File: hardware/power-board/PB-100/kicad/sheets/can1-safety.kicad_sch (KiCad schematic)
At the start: 0 parts

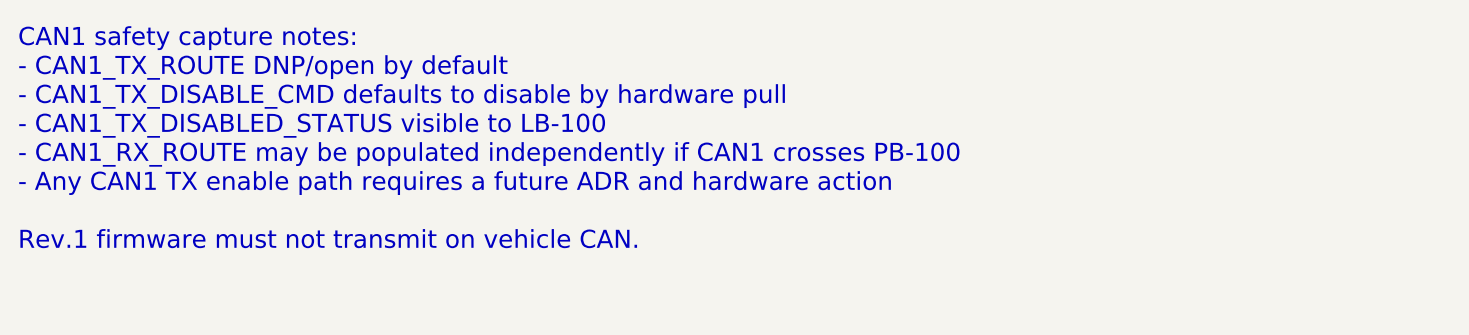
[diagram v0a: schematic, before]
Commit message: hardware: tighten pb100 can1 disable contract
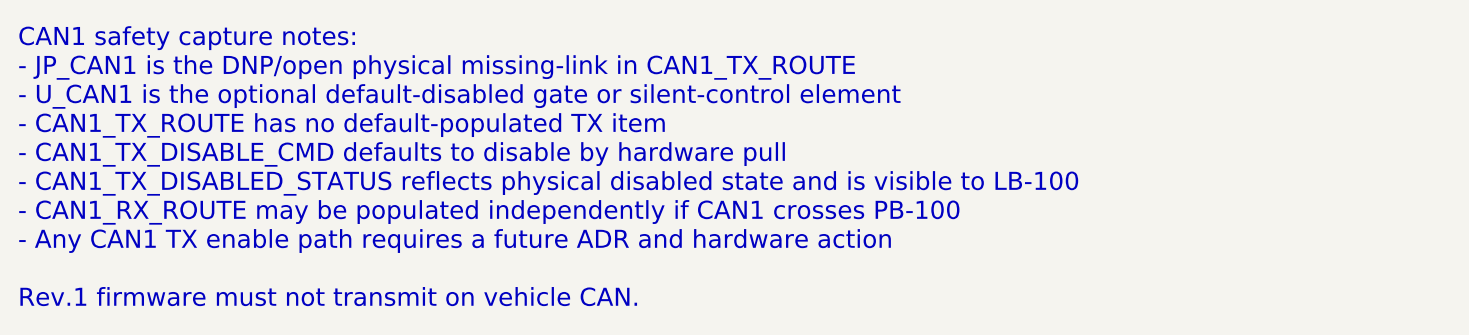
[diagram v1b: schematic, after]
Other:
- note added: "CAN1 safety capture notes: - JP_CAN1 is the DNP/open physical missing-link in CAN1_TX_ROUTE - U_CAN1 is the optional default-disabled gate or silent-control element - CAN1_TX_ROUTE has no default-populated TX item - CAN1_TX_DISABLE_CMD defaults to disable by hardware pull - CAN1_TX_DISABLED_STATUS reflects physical disabled state and is visible to LB-100 - CAN1_RX_ROUTE may be populated independe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"
- note removed: "CAN1 safety capture notes: - CAN1_TX_ROUTE DNP/open by default - CAN1_TX_DISABLE_CMD defaults to disable by hardware pull - CAN1_TX_DISABLED_STATUS visible to LB-100 - CAN1_RX_ROUTE may be populated independently if CAN1 crosses PB-100 - Any CAN1 TX enable path requires a future ADR and hardware action Rev.1 firmware must not transmit on vehicle CAN."
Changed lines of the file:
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@@
     (company "SVC Platform")
     (comment 9 "Work queue: CAP-CAN1. CAN1 capture keeps TX DNP/open and future ADR only.")
-    (comment 1 "Placeholder sheet. Capture CAN1 TX disable/DNP-open path here.")
+    (comment 1 "Capture contract: JP_CAN1 DNP/open TX link and U_CAN1 default-disabled gate.")
     (comment 2 "Source: PB-100-can1-tx-disable.md.")
   )
-  (text "CAN1 safety capture notes:\n- CAN1_TX_ROUTE DNP/open by default\n- CAN1_TX_DISABLE_CMD defaults to disable by hardware pull\n- CAN1_TX_DISABLED_STATUS visible to LB-100\n- CAN1_RX_ROUTE may be populated independently if CAN1 crosses PB-100\n- Any CAN1 TX enable path requires a future ADR and hardware action\n\nRev.1 firmware must not transmit on vehicle CAN."
+  (text "CAN1 safety capture notes:\n- JP_CAN1 is the DNP/open physical missing-link in CAN1_TX_ROUTE\n- U_CAN1 is the optional default-disabled gate or silent-control element\n- CAN1_TX_ROUTE has no default-populated TX item\n- CAN1_TX_DISABLE_CMD defaults to disable by hardware pull\n- CAN1_TX_DISABLED_STATUS reflects physical disabled state and is visible to LB-100\n- CAN1_RX_ROUTE may be populated independently if CAN1 crosses PB-100\n- Any CAN1 TX enable path requires a future ADR and hardware action\n\nRev.1 firmware must not transmit on vehicle CAN."
     (at 25 30 0)
     (effects (font (size 2.0 2.0)) (justify left top))

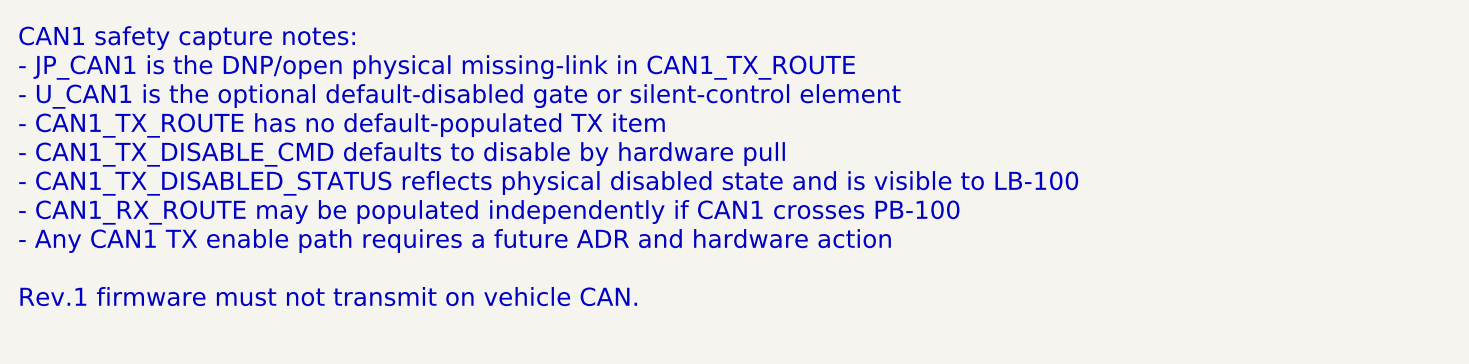
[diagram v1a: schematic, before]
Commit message: hardware: sync pb100 kicad sheet trace notes
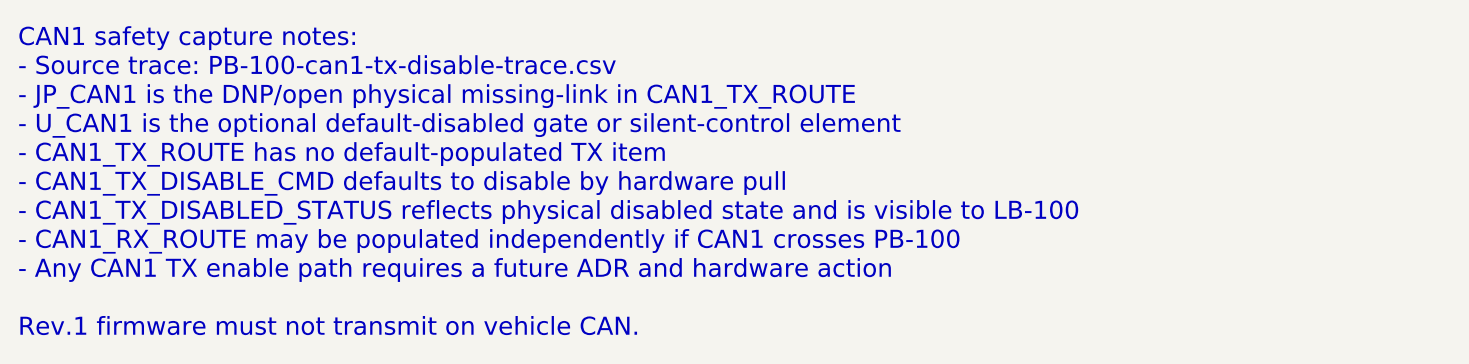
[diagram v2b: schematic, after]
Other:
- note added: "CAN1 safety capture notes: - Source trace: PB-100-can1-tx-disable-trace.csv - JP_CAN1 is the DNP/open physical missing-link in CAN1_TX_ROUTE - U_CAN1 is the optional default-disabled gate or silent-control element - CAN1_TX_ROUTE has no default-populated TX item - CAN1_TX_DISABLE_CMD defaults to disable by hardware pull - CAN1_TX_DISABLED_STATUS reflects physical disabled state and is visible to 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"
- note removed: "CAN1 safety capture notes: - JP_CAN1 is the DNP/open physical missing-link in CAN1_TX_ROUTE - U_CAN1 is the optional default-disabled gate or silent-control element - CAN1_TX_ROUTE has no default-populated TX item - CAN1_TX_DISABLE_CMD defaults to disable by hardware pull - CAN1_TX_DISABLED_STATUS reflects physical disabled state and is visible to LB-100 - CAN1_RX_ROUTE may be populated independe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"
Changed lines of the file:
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@@
     (comment 9 "Work queue: CAP-CAN1. CAN1 capture keeps TX DNP/open and future ADR only.")
     (comment 1 "Capture contract: JP_CAN1 DNP/open TX link and U_CAN1 default-disabled gate.")
-    (comment 2 "Source: PB-100-can1-tx-disable.md.")
+    (comment 2 "Sources: PB-100-can1-tx-disable-trace.csv and PB-100-can1-tx-disable.md.")
   )
-  (text "CAN1 safety capture notes:\n- JP_CAN1 is the DNP/open physical missing-link in CAN1_TX_ROUTE\n- U_CAN1 is the optional default-disabled gate or silent-control element\n- CAN1_TX_ROUTE has no default-populated TX item\n- CAN1_TX_DISABLE_CMD defaults to disable by hardware pull\n- CAN1_TX_DISABLED_STATUS reflects physical disabled state and is visible to LB-100\n- CAN1_RX_ROUTE may be populated independently if CAN1 crosses PB-100\n- Any CAN1 TX enable path requires a future ADR and hardware action\n\nRev.1 firmware must not transmit on vehicle CAN."
+  (text "CAN1 safety capture notes:\n- Source trace: PB-100-can1-tx-disable-trace.csv\n- JP_CAN1 is the DNP/open physical missing-link in CAN1_TX_ROUTE\n- U_CAN1 is the optional default-disabled gate or silent-control element\n- CAN1_TX_ROUTE has no default-populated TX item\n- CAN1_TX_DISABLE_CMD defaults to disable by hardware pull\n- CAN1_TX_DISABLED_STATUS reflects physical disabled state and is visible to LB-100\n- CAN1_RX_ROUTE may be populated independently if CAN1 crosses PB-100\n- Any CAN1 TX enable path requires a future ADR and hardware action\n\nRev.1 firmware must not transmit on vehicle CAN."
     (at 25 30 0)
     (effects (font (size 2.0 2.0)) (justify left top))

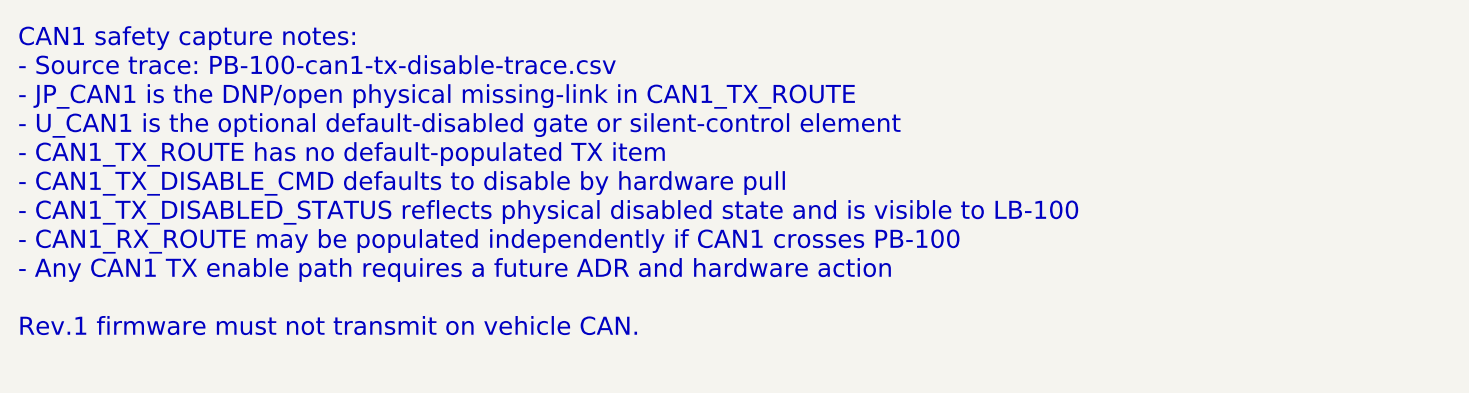
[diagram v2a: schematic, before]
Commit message: hardware: add pb100 can1 dnp production review
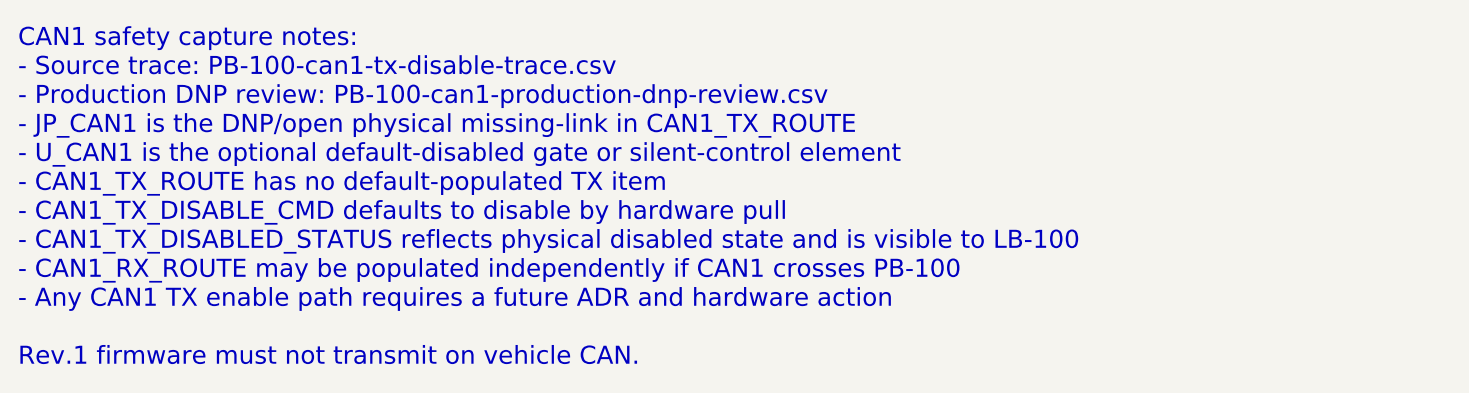
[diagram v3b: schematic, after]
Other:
- note added: "CAN1 safety capture notes: - Source trace: PB-100-can1-tx-disable-trace.csv - Production DNP review: PB-100-can1-production-dnp-review.csv - JP_CAN1 is the DNP/open physical missing-link in CAN1_TX_ROUTE - U_CAN1 is the optional default-disabled gate or silent-control element - CAN1_TX_ROUTE has no default-populated TX item - CAN1_TX_DISABLE_CMD defaults to disable by hardware pull - CAN1_TX_DISA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"
- note removed: "CAN1 safety capture notes: - Source trace: PB-100-can1-tx-disable-trace.csv - JP_CAN1 is the DNP/open physical missing-link in CAN1_TX_ROUTE - U_CAN1 is the optional default-disabled gate or silent-control element - CAN1_TX_ROUTE has no default-populated TX item - CAN1_TX_DISABLE_CMD defaults to disable by hardware pull - CAN1_TX_DISABLED_STATUS reflects physical disabled state and is visible to 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"
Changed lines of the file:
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@@
     (comment 9 "Work queue: CAP-CAN1. CAN1 capture keeps TX DNP/open and future ADR only.")
     (comment 1 "Capture contract: JP_CAN1 DNP/open TX link and U_CAN1 default-disabled gate.")
-    (comment 2 "Sources: PB-100-can1-tx-disable-trace.csv and PB-100-can1-tx-disable.md.")
+    (comment 2 "Sources: PB-100-can1-tx-disable-trace.csv, PB-100-can1-production-dnp-review.csv, and PB-100-can1-tx-disable.md.")
   )
-  (text "CAN1 safety capture notes:\n- Source trace: PB-100-can1-tx-disable-trace.csv\n- JP_CAN1 is the DNP/open physical missing-link in CAN1_TX_ROUTE\n- U_CAN1 is the optional default-disabled gate or silent-control element\n- CAN1_TX_ROUTE has no default-populated TX item\n- CAN1_TX_DISABLE_CMD defaults to disable by hardware pull\n- CAN1_TX_DISABLED_STATUS reflects physical disabled state and is visible to LB-100\n- CAN1_RX_ROUTE may be populated independently if CAN1 crosses PB-100\n- Any CAN1 TX enable path requires a future ADR and hardware action\n\nRev.1 firmware must not transmit on vehicle CAN."
+  (text "CAN1 safety capture notes:\n- Source trace: PB-100-can1-tx-disable-trace.csv\n- Production DNP review: PB-100-can1-production-dnp-review.csv\n- JP_CAN1 is the DNP/open physical missing-link in CAN1_TX_ROUTE\n- U_CAN1 is the optional default-disabled gate or silent-control element\n- CAN1_TX_ROUTE has no default-populated TX item\n- CAN1_TX_DISABLE_CMD defaults to disable by hardware pull\n- CAN1_TX_DISABLED_STATUS reflects physical disabled state and is visible to LB-100\n- CAN1_RX_ROUTE may be populated independently if CAN1 crosses PB-100\n- Any CAN1 TX enable path requires a future ADR and hardware action\n\nRev.1 firmware must not transmit on vehicle CAN."
     (at 25 30 0)
     (effects (font (size 2.0 2.0)) (justify left top))
